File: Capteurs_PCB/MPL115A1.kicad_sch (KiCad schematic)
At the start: 2 parts, among them U1 MPL115A1

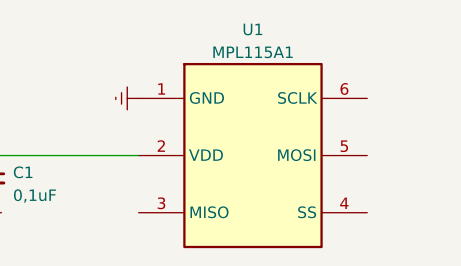
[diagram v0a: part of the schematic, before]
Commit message: PCB changement
Pcb changé (Raspberry))
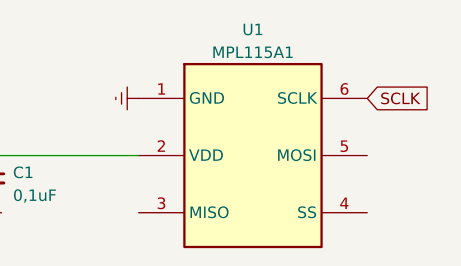
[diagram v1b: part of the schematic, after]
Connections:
- net SCLK: now reaches U1.6 (SCLK)
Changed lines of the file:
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@@
     (stroke (width 0) (type default))
+  )
+  (global_label "SCLK" (shape input) (at 143.51 96.52 0) (fields_autoplaced)
+    (effects (font (size 1.27 1.27)) (justify left))
+    (property "Intersheetrefs" "${INTERSHEET_REFS}" (at 151.1934 96.52 0)
+      (effects (font (size 1.27 1.27)) (justify left) hide)
+    )
   )
   (global_label "VDD" (shape input) (at 95.25 102.87 180) (fields_autoplaced)

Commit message: pcb update
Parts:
- removed U1: MPL115A1, Package_LGA:NXP_LGA-8_3x5mm_P1.25mm_H1.2mm, symbol Sensor_Pressure:MPL115A1
- added U6: MPL115A1, Package_LGA:NXP_LGA-8_3x5mm_P1.25mm_H1.2mm, symbol Sensor_Pressure:MPL115A1
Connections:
- net Earth: now also U6.1 (GND)
- net SCLK: now also U6.6 (SCLK)
- net VDD renamed VDD_P
- net VDD_P: now also U6.2 (VDD)
- new net MISO: U6.3 (MISO)
- new net MOSI: U6.5 (MOSI)
- new net SS: U6.4 (SS)
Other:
- moved on the sheet: C1
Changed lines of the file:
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@@
 (kicad_sch (version 20230121) (generator eeschema)
   (paper "A4")
-  (junction (at 101.6 102.87) (diameter 0) (color 0 0 0 0)
+  (junction (at 133.35 77.47) (diameter 0) (color 0 0 0 0)
   )
-  (wire (pts (xy 95.25 102.87) (xy 101.6 102.87))
+  (wire (pts (xy 133.35 71.12) (xy 133.35 77.47))
     (stroke (width 0) (type default))
   )
-  (wire (pts (xy 101.6 102.87) (xy 118.11 102.87))
+  (wire (pts (xy 133.35 77.47) (xy 133.35 86.36))
     (stroke (width 0) (type default))
   )
-  (global_label "SCLK" (shape input) (at 143.51 96.52 0) (fields_autoplaced)
+  (global_label "MISO" (shape input) (at 120.65 101.6 180) (fields_autoplaced)
+    (effects (font (size 1.27 1.27)) (justify right))
+    (property "Intersheetrefs" "${INTERSHEET_REFS}" (at 113.148 101.6 0)
+      (effects (font (size 1.27 1.27)) (justify right) hide)
+    )
+  )
+  (global_label "SS" (shape input) (at 120.65 104.14 180) (fields_autoplaced)
+    (effects (font (size 1.27 1.27)) (justify right))
+    (property "Intersheetrefs" "${INTERSHEET_REFS}" (at 115.3252 104.14 0)
+      (effects (font (size 1.27 1.27)) (justify right) hide)
+    )
+  )
+  (global_label "SCLK" (shape input) (at 120.65 96.52 180) (fields_autoplaced)
+    (effects (font (size 1.27 1.27)) (justify right))
+    (property "Intersheetrefs" "${INTERSHEET_REFS}" (at 112.9666 96.52 0)
+      (effects (font (size 1.27 1.27)) (justify right) hide)
+    )
+  )
+  (global_label "MOSI" (shape input) (at 120.65 99.06 180) (fields_autoplaced)
+    (effects (font (size 1.27 1.27)) (justify right))
+    (property "Intersheetrefs" "${INTERSHEET_REFS}" (at 113.148 99.06 0)
+      (effects (font (size 1.27 1.27)) (justify right) hide)
+    )
+  )
+  (global_label "VDD_P" (shape input) (at 133.35 71.12 90) (fields_autoplaced)
     (effects (font (size 1.27 1.27)) (justify left))
-    (property "Intersheetrefs" "${INTERSHEET_REFS}" (at 151.1934 96.52 0)
+    (property "Intersheetrefs" "${INTERSHEET_REFS}" (at 133.35 62.348 90)
       (effects (font (size 1.27 1.27)) (justify left) hide)
     )
   )
-  (global_label "VDD" (shape input) (at 95.25 102.87 180) (fields_autoplaced)
-    (effects (font (size 1.27 1.27)) (justify right))
-    (property "Intersheetrefs" "${INTERSHEET_REFS}" (at 88.7156 102.87 0)
-      (effects (font (size 1.27 1.27)) (justify right) hide)
+  (symbol (lib_name "MPL115A1_1") (lib_id "Sensor_Pressure:MPL115A1") (at 133.35 101.6 0) (unit 1)
+    (in_bom yes) (on_board yes) (dnp no) (fields_autoplaced)
+    (property "Reference" "U6" (at 142.24 100.965 0)
+      (effects (font (size 1.27 1.27)) (justify left))
     )
-  )
-  (symbol (lib_id "Sensor_Pressure:MPL115A1") (at 130.81 102.87 90) (unit 1)
-    (in_bom yes) (on_board yes) (dnp no) (fields_autoplaced)
-    (property "Reference" "U1" (at 130.81 88.9 90)
-      (effects (font (size 1.27 1.27)))
+    (property "Value" "MPL115A1" (at 142.24 103.505 0)
+      (effects (font (size 1.27 1.27)) (justify left))
     )
-    (property "Value" "MPL115A1" (at 130.81 91.44 90)
-      (effects (font (size 1.27 1.27)))
-    )
-    (property "Footprint" "Package_LGA:NXP_LGA-8_3x5mm_P1.25mm_H1.2mm" (at 157.48 101.6 0)
+    (property "Footprint" "Package_LGA:NXP_LGA-8_3x5mm_P1.25mm_H1.2mm" (at 134.62 66.04 0)
       (effects (font (size 1.27 1.27)) hide)
     )
-    (property "Datasheet" "http://www.nxp.com/assets/documents/data/en/data-sheets/MPL115A1.pdf" (at 161.29 102.87 0)
+    (property "Datasheet" "http://www.nxp.com/assets/documents/data/en/data-sheets/MPL115A1.pdf" (at 133.35 69.85 0)
       (effects (font (size 1.27 1.27)) hide)
     )
@@
     (instances
       (project "Capteurs_PCB"
-        (path "/1101af8f-9425-4102-9245-339dc54562bf"
-          (reference "U1") (unit 1)
-        )
         (path "/1101af8f-9425-4102-9245-339dc54562bf/3d971057-5943-41d9-af92-399a5cf9d777"
-          (reference "U1") (unit 1)
+          (reference "U6") (unit 1)
         )
       )
     )
   )
-  (symbol (lib_id "power:Earth") (at 101.6 107.95 0) (unit 1)
+  (symbol (lib_id "power:Earth") (at 128.27 77.47 270) (unit 1)
     (in_bom yes) (on_board yes) (dnp no) (fields_autoplaced)
-    (property "Reference" "#PWR01" (at 101.6 114.3 0)
+    (property "Reference" "#PWR01" (at 121.92 77.47 0)
       (effects (font (size 1.27 1.27)) hide)
     )
-    (property "Value" "Earth" (at 101.6 111.76 0)
+    (property "Value" "Earth" (at 124.46 77.47 0)
       (effects (font (size 1.27 1.27)) hide)
     )
-    (property "Footprint" "" (at 101.6 107.95 0)
+    (property "Footprint" "" (at 128.27 77.47 0)
       (effects (font (size 1.27 1.27)) hide)
     )
-    (property "Datasheet" "~" (at 101.6 107.95 0)
+    (property "Datasheet" "~" (at 128.27 77.47 0)
       (effects (font (size 1.27 1.27)) hide)
     )
@@
     )
   )
-  (symbol (lib_id "Device:C_Small") (at 101.6 105.41 0) (unit 1)
+  (symbol (lib_id "Device:C_Small") (at 130.81 77.47 270) (unit 1)
     (in_bom yes) (on_board yes) (dnp no) (fields_autoplaced)
-    (property "Reference" "C1" (at 104.14 104.7813 0)
+    (property "Reference" "C1" (at 131.4387 80.01 0)
       (effects (font (size 1.27 1.27)) (justify left))
     )
-    (property "Value" "0,1uF" (at 104.14 107.3213 0)
+    (property "Value" "0,1uF" (at 128.8987 80.01 0)
       (effects (font (size 1.27 1.27)) (justify left))
     )
-    (property "Footprint" "" (at 101.6 105.41 0)
+    (property "Footprint" "" (at 130.81 77.47 0)
       (effects (font (size 1.27 1.27)) hide)
     )
-    (property "Datasheet" "~" (at 101.6 105.41 0)
+    (property "Datasheet" "~" (at 130.81 77.47 0)
       (effects (font (size 1.27 1.27)) hide)
     )
@@
     )
   )
-  (symbol (lib_id "power:Earth") (at 118.11 96.52 270) (unit 1)
+  (symbol (lib_id "power:Earth") (at 133.35 116.84 0) (unit 1)
     (in_bom yes) (on_board yes) (dnp no) (fields_autoplaced)
-    (property "Reference" "#PWR02" (at 111.76 96.52 0)
+    (property "Reference" "#PWR02" (at 133.35 123.19 0)
       (effects (font (size 1.27 1.27)) hide)
     )
-    (property "Value" "Earth" (at 114.3 96.52 0)
+    (property "Value" "Earth" (at 133.35 120.65 0)
       (effects (font (size 1.27 1.27)) hide)
     )
-    (property "Footprint" "" (at 118.11 96.52 0)
+    (property "Footprint" "" (at 133.35 116.84 0)
       (effects (font (size 1.27 1.27)) hide)
     )
-    (property "Datasheet" "~" (at 118.11 96.52 0)
+    (property "Datasheet" "~" (at 133.35 116.84 0)
       (effects (font (size 1.27 1.27)) hide)
     )

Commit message: updates pcb
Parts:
- C1: value 0,1uF -> 100nF; footprint (none) -> Capacitor_SMD:C_1206_3216Metric
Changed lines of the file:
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@@
   (symbol (lib_id "Device:C_Small") (at 130.81 77.47 270) (unit 1)
     (in_bom yes) (on_board yes) (dnp no) (fields_autoplaced)
-    (property "Reference" "C1" (at 131.4387 80.01 0)
-      (effects (font (size 1.27 1.27)) (justify left))
+    (property "Reference" "C1" (at 130.8036 72.39 90)
+      (effects (font (size 1.27 1.27)))
     )
-    (property "Value" "0,1uF" (at 128.8987 80.01 0)
-      (effects (font (size 1.27 1.27)) (justify left))
+    (property "Value" "100nF" (at 130.8036 74.93 90)
+      (effects (font (size 1.27 1.27)))
     )
-    (property "Footprint" "" (at 130.81 77.47 0)
+    (property "Footprint" "Capacitor_SMD:C_1206_3216Metric" (at 130.81 77.47 0)
       (effects (font (size 1.27 1.27)) hide)
     )

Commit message: Modif PCB
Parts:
- U6: value MPL115A1 -> 32350268; footprint Package_LGA:NXP_LGA-8_3x5mm_P1.25mm_H1.2mm -> (none)
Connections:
- net Earth: no longer names the net of C1.2
- net Earth: no longer U6.1 (GND)
- net VDD_P renamed VDD
- new net GND: U6.1 (GND)
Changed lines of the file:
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@@
     (stroke (width 0) (type default))
   )
-  (global_label "MISO" (shape input) (at 120.65 101.6 180) (fields_autoplaced)
+  (hierarchical_label "SS" (shape input) (at 120.65 104.14 180) (fields_autoplaced)
     (effects (font (size 1.27 1.27)) (justify right))
-    (property "Intersheetrefs" "${INTERSHEET_REFS}" (at 113.148 101.6 0)
-      (effects (font (size 1.27 1.27)) (justify right) hide)
-    )
   )
-  (global_label "SS" (shape input) (at 120.65 104.14 180) (fields_autoplaced)
+  (hierarchical_label "MOSI" (shape input) (at 120.65 99.06 180) (fields_autoplaced)
     (effects (font (size 1.27 1.27)) (justify right))
-    (property "Intersheetrefs" "${INTERSHEET_REFS}" (at 115.3252 104.14 0)
-      (effects (font (size 1.27 1.27)) (justify right) hide)
-    )
   )
-  (global_label "SCLK" (shape input) (at 120.65 96.52 180) (fields_autoplaced)
+  (hierarchical_label "MISO" (shape input) (at 120.65 101.6 180) (fields_autoplaced)
     (effects (font (size 1.27 1.27)) (justify right))
-    (property "Intersheetrefs" "${INTERSHEET_REFS}" (at 112.9666 96.52 0)
-      (effects (font (size 1.27 1.27)) (justify right) hide)
-    )
   )
-  (global_label "MOSI" (shape input) (at 120.65 99.06 180) (fields_autoplaced)
+  (hierarchical_label "SCLK" (shape input) (at 120.65 96.52 180) (fields_autoplaced)
     (effects (font (size 1.27 1.27)) (justify right))
-    (property "Intersheetrefs" "${INTERSHEET_REFS}" (at 113.148 99.06 0)
-      (effects (font (size 1.27 1.27)) (justify right) hide)
-    )
   )
-  (global_label "VDD_P" (shape input) (at 133.35 71.12 90) (fields_autoplaced)
+  (hierarchical_label "VDD" (shape input) (at 133.35 71.12 90) (fields_autoplaced)
     (effects (font (size 1.27 1.27)) (justify left))
-    (property "Intersheetrefs" "${INTERSHEET_REFS}" (at 133.35 62.348 90)
-      (effects (font (size 1.27 1.27)) (justify left) hide)
-    )
   )
   (symbol (lib_name "MPL115A1_1") (lib_id "Sensor_Pressure:MPL115A1") (at 133.35 101.6 0) (unit 1)
@@
       (effects (font (size 1.27 1.27)) (justify left))
     )
-    (property "Value" "MPL115A1" (at 142.24 103.505 0)
+    (property "Value" "32350268" (at 142.24 103.505 0)
       (effects (font (size 1.27 1.27)) (justify left))
     )
-    (property "Footprint" "Package_LGA:NXP_LGA-8_3x5mm_P1.25mm_H1.2mm" (at 134.62 66.04 0)
+    (property "Footprint" "" (at 134.62 66.04 0)
       (effects (font (size 1.27 1.27)) hide)
     )
-    (property "Datasheet" "http://www.nxp.com/assets/documents/data/en/data-sheets/MPL115A1.pdf" (at 133.35 69.85 0)
+    (property "Datasheet" "https://prod-edam.honeywell.com/content/dam/honeywell-edam/sps/siot/en-us/products/sensors/pressure-sensors/board-mount-pressure-sensors/basic-abp2-series/documents/sps-siot-abp2-series-datasheet-32350268-en.pdf" (at 133.35 69.85 0)
       (effects (font (size 1.27 1.27)) hide)
     )
@@
     )
   )
-  (symbol (lib_id "power:Earth") (at 128.27 77.47 270) (unit 1)
+  (symbol (lib_id "power:GND") (at 133.35 116.84 0) (unit 1)
     (in_bom yes) (on_board yes) (dnp no) (fields_autoplaced)
-    (property "Reference" "#PWR02" (at 121.92 77.47 0)
+    (property "Reference" "#PWR02" (at 133.35 123.19 0)
       (effects (font (size 1.27 1.27)) hide)
     )
-    (property "Value" "Earth" (at 124.46 77.47 0)
+    (property "Value" "GND" (at 133.35 121.92 0)
+      (effects (font (size 1.27 1.27)))
+    )
+    (property "Footprint" "" (at 133.35 116.84 0)
       (effects (font (size 1.27 1.27)) hide)
     )
-    (property "Footprint" "" (at 128.27 77.47 0)
-      (effects (font (size 1.27 1.27)) hide)
-    )
-    (property "Datasheet" "~" (at 128.27 77.47 0)
+    (property "Datasheet" "" (at 133.35 116.84 0)
       (effects (font (size 1.27 1.27)) hide)
     )
@@
         )
       )
-    )
-  )
-  (symbol (lib_id "power:Earth") (at 133.35 116.84 0) (unit 1)
-    (in_bom yes) (on_board yes) (dnp no) (fields_autoplaced)
-    (property "Reference" "#PWR01" (at 133.35 123.19 0)
-      (effects (font (size 1.27 1.27)) hide)
-    )
-    (property "Value" "Earth" (at 133.35 120.65 0)
-      (effects (font (size 1.27 1.27)) hide)
-    )
-    (property "Footprint" "" (at 133.35 116.84 0)
-      (effects (font (size 1.27 1.27)) hide)
-    )
-    (property "Datasheet" "~" (at 133.35 116.84 0)
-      (effects (font (size 1.27 1.27)) hide)
-    )
-    (pin "1")
-    (instances
-      (project "Capteurs_PCB"
-        (path "/1101af8f-9425-4102-9245-339dc54562bf/3d971057-5943-41d9-af92-399a5cf9d777"
-          (reference "#PWR01") (unit 1)
-        )
-      )

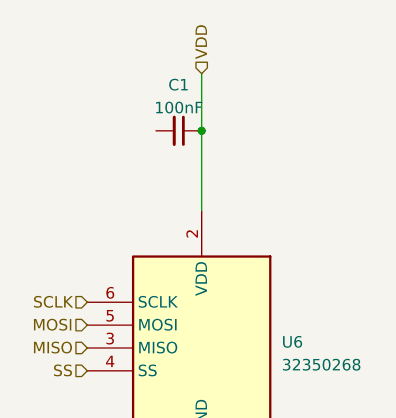
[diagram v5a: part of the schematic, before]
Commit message: kicad changes and starting footprints
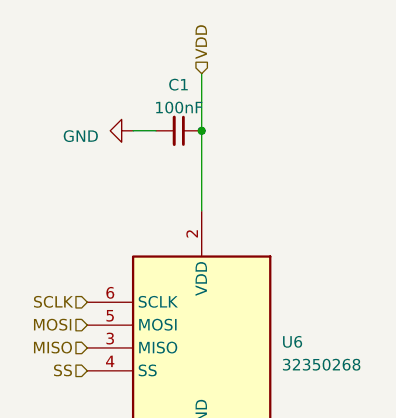
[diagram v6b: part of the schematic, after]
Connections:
- net GND: now also C1.2
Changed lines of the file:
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@@
+    (stroke (width 0) (type default))
+  )
+  (wire (pts (xy 125.73 77.47) (xy 128.27 77.47))
     (stroke (width 0) (type default))
   )
@@
         )
       )
+    )
+  )
+  (symbol (lib_id "power:GND") (at 125.73 77.47 270) (unit 1)
+    (in_bom yes) (on_board yes) (dnp no) (fields_autoplaced)
+    (property "Reference" "#PWR027" (at 119.38 77.47 0)
+      (effects (font (size 1.27 1.27)) hide)
+    )
+    (property "Value" "GND" (at 121.92 78.105 90)
+      (effects (font (size 1.27 1.27)) (justify right))
+    )
+    (property "Footprint" "" (at 125.73 77.47 0)
+      (effects (font (size 1.27 1.27)) hide)
+    )
+    (property "Datasheet" "" (at 125.73 77.47 0)
+      (effects (font (size 1.27 1.27)) hide)
+    )
+    (pin "1")
+    (instances
+      (project "Capteurs_PCB"
+        (path "/1101af8f-9425-4102-9245-339dc54562bf/3d971057-5943-41d9-af92-399a5cf9d777"
+          (reference "#PWR027") (unit 1)
+        )
+      )
